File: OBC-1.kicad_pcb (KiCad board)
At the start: 6 copper layers, 42.8 x 42.8 mm, 110 parts, among them J1 ERM8-020-X, J2 ERF6-020-X, J3 Conn_01x02_Female, Q1 MGSF1N02L, Q2 MGSF1N02L, U1 TPS62850x-Q1, U11 TMS5701227CZWTQQ1, U2 TPS62850x-Q1, U3 LTC4353, U4 SN65HVD230M-EP, U5 SN65HVD230M-EP, U6 SN65HVD230M-EP

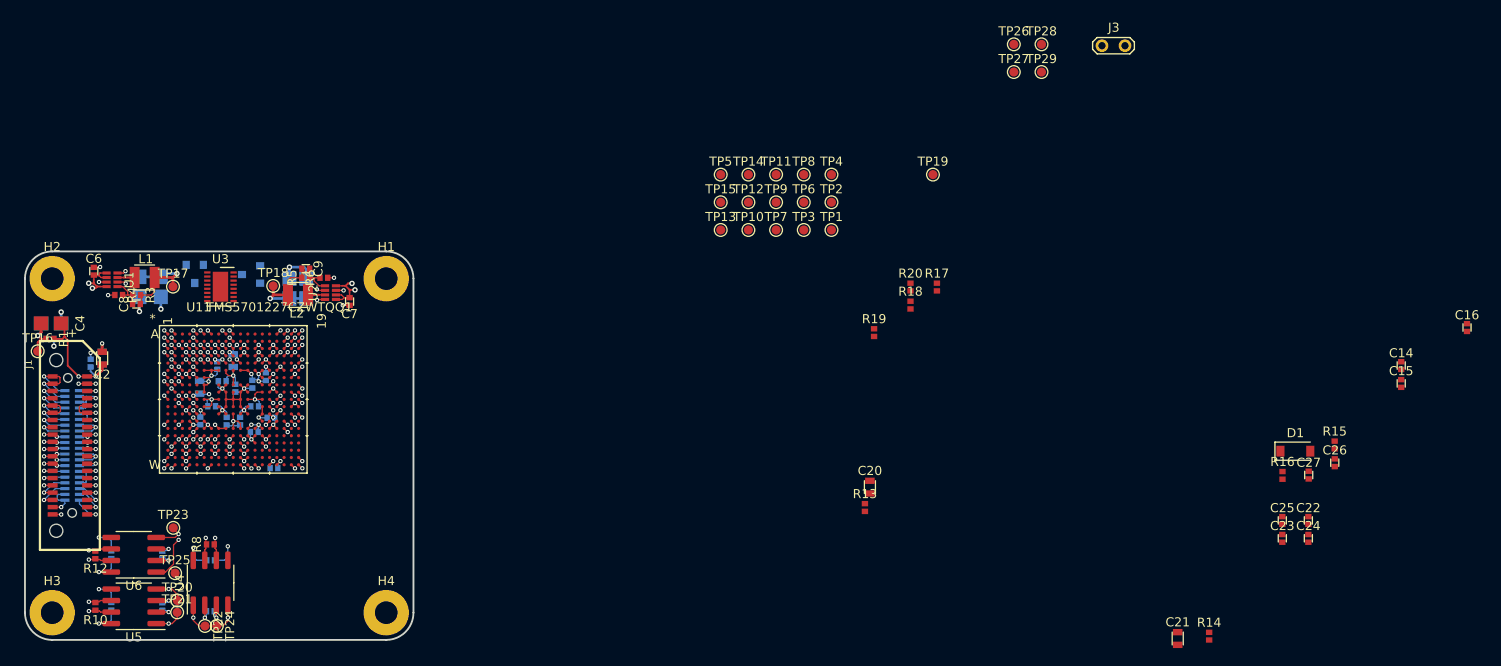
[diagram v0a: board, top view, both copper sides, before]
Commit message: progressed power supply layout, added 3D models to footprints
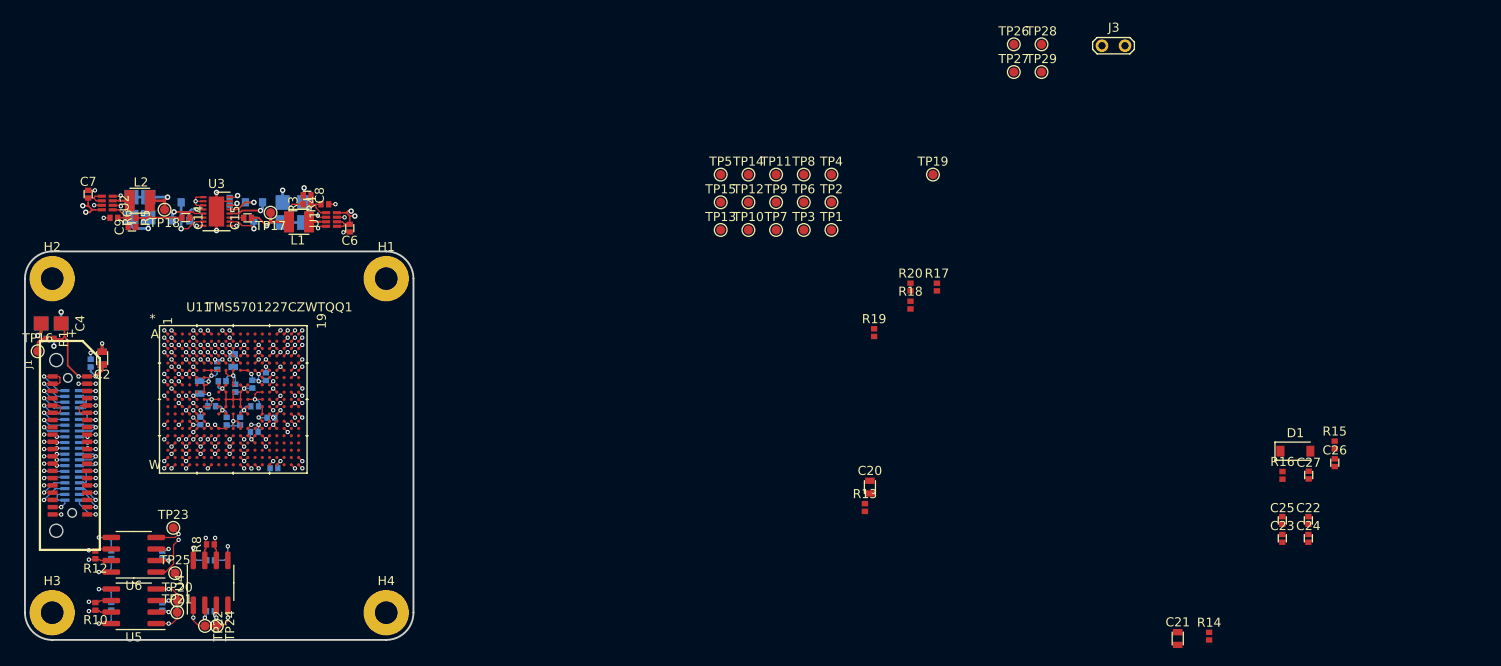
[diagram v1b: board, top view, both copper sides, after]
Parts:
- C16: moved to B.Cu
- moved C16 137.0 mm to (111.5, 66.0), turned to 180 degrees
- moved C14 134.9 mm to (106.6, 67.8), turned to 270 degrees
- moved C15 128.4 mm to (113.5, 67.8), turned to 90 degrees
- moved C7 31.1 mm to (95.9, 65.2), turned to 0 degrees
- moved C6 28.6 mm to (124.7, 68.9), turned to 180 degrees
- moved U2 28.2 mm to (97.4, 65.4), turned to 270 degrees
- moved U1 25.9 mm to (123.3, 68.7), turned to 90 degrees
- moved R4 24.8 mm to (121.9, 66.3), turned to 90 degrees
- moved R6 24.1 mm to (98.7, 67.8), turned to 270 degrees
- moved C8 22.3 mm to (120.0, 65.3), turned to 270 degrees
- moved R3 21.2 mm to (120.0, 66.3), turned to 90 degrees
- moved C11 21.2 mm to (100.6, 66.6), turned to 180 degrees
- moved L2 20.3 mm to (101.6, 65.9), turned to 0 degrees
- moved R5 20.3 mm to (100.7, 67.8), turned to 270 degrees
- moved C10 19.9 mm to (119.7, 67.2), turned to 0 degrees
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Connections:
- U11 pad C1: /TMS570_uC/OBC_1V25_P_PG -> /Power/OBC_1V25_P_PG
- U11 pad C2: /TMS570_uC/OBC_1V25_R_PG -> /Power/OBC_1V25_R_PG
- U3 pad 8: /Power/OBC_1V2_R_PG -> /Power/OBC_1V25_R_PG
- U3 pad 9: /Power/OBC_1V2_P_PG -> /Power/OBC_1V25_P_PG
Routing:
- net GND: track 178.0 -> 190.0 mm, vias 119 -> 123
- net OBC_1V2_R: track 11.4 -> 21.4 mm, vias 1 -> 2
- net OBC_1V25: track 19.5 -> 29.1 mm, vias 4 -> 6
- net OBC_1V25_P: track 12.0 -> 21.3 mm, vias 1 -> 2
- net /Power/GATE_1: track 0.00 -> 4.53 mm, vias 0 -> 1
- net /Power/GATE_2: track 0.00 -> 4.32 mm, vias 0 -> 1
- net OBC_3V3: track 65.6 -> 67.4 mm, vias 23 -> 24
- net Net-(C15-Pad2): track 0.00 -> 1.56 mm
- net Net-(C14-Pad2): track 0.00 -> 1.50 mm
- net /Power/OBC_1V25_P_PG: track 0.00 -> 1.31 mm, vias 0 -> 2
- net /Power/OBC_1V25_R_PG: track 0.00 -> 1.29 mm, vias 0 -> 2
- net /TMS570_uC/OBC_1V25_R_PG: track 0.57 -> 0.00 mm, vias 1 -> 0
- net /TMS570_uC/OBC_1V25_P_PG: track 0.56 -> 0.00 mm, vias 1 -> 0

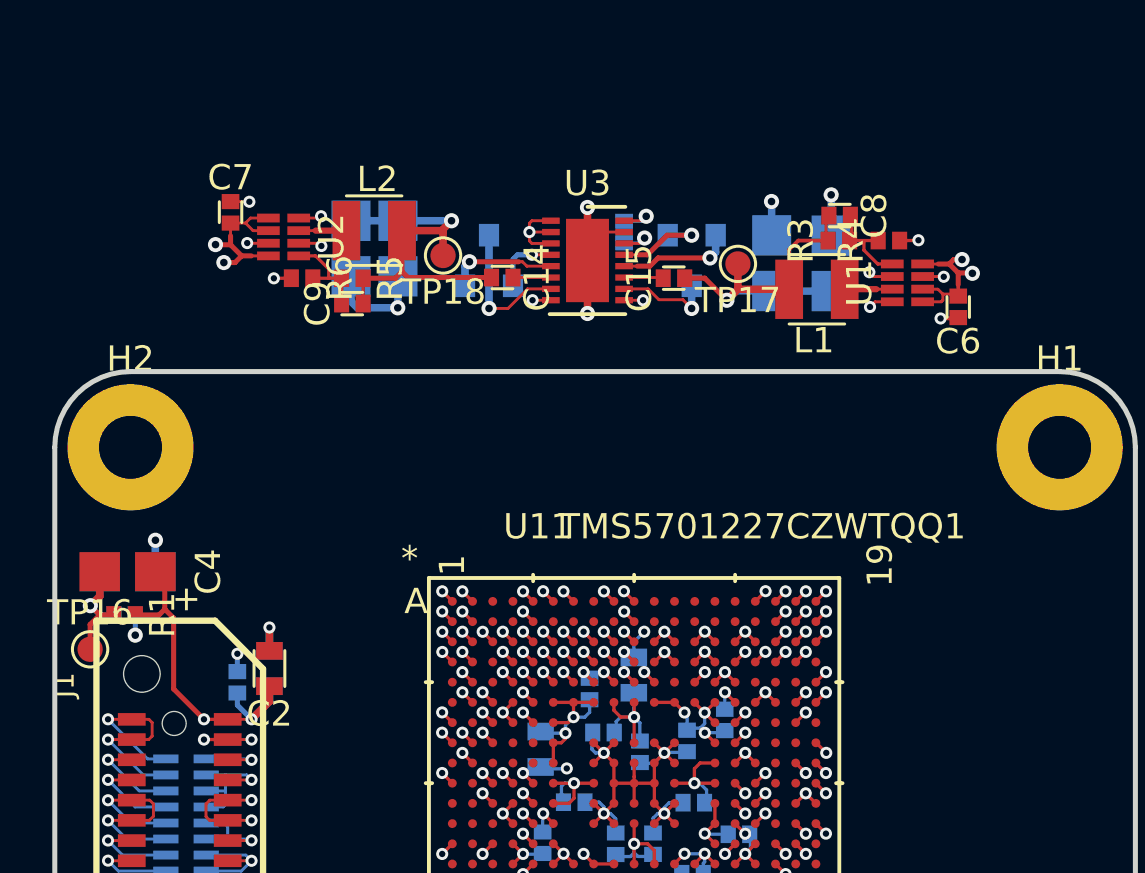
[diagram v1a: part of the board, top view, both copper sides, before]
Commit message: updated power planes
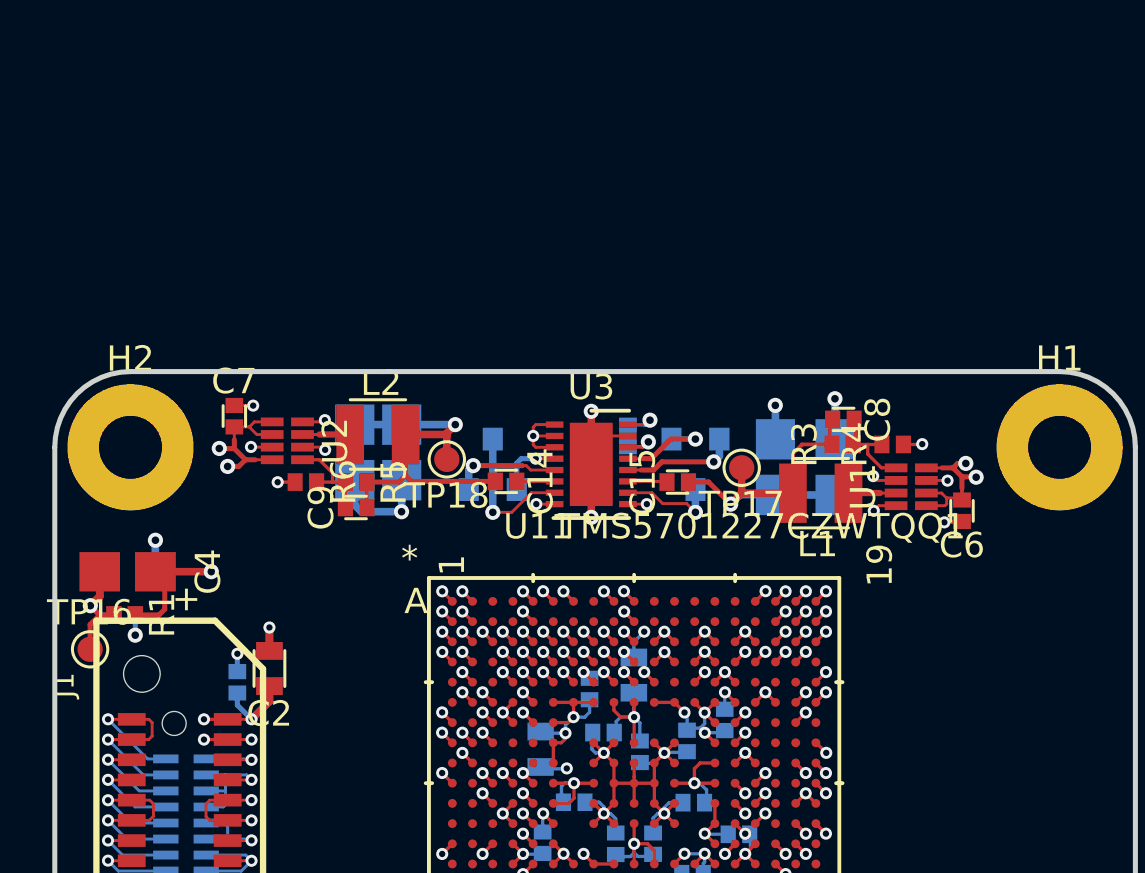
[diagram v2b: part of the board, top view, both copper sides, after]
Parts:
- moved C10 8.08 mm to (119.8, 75.3)
- moved C11 8.08 mm to (100.8, 74.7)
- moved C12 8.08 mm to (117.4, 75.3)
- moved C13 8.08 mm to (102.6, 74.7)
- moved C15 8.08 mm to (113.6, 75.9)
- moved C16 8.08 mm to (111.6, 74.1)
- moved C6 8.08 mm to (124.8, 77.0)
- moved C7 8.08 mm to (96.0, 73.3)
- moved C8 8.08 mm to (120.1, 73.4)
- moved C9 8.08 mm to (100.9, 76.9)
- moved L1 8.08 mm to (119.2, 76.3)
- moved Q1 8.08 mm to (106.2, 75.2)
- moved Q2 8.08 mm to (114.3, 75.2)
- moved R3 8.08 mm to (120.1, 74.4)
- moved R4 8.08 mm to (122.1, 74.4)
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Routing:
- net OBC_3V3: track 67.4 -> 64.6 mm, vias 24 -> 25
- removed copper zone on In3.Cu, net OBC_3V3

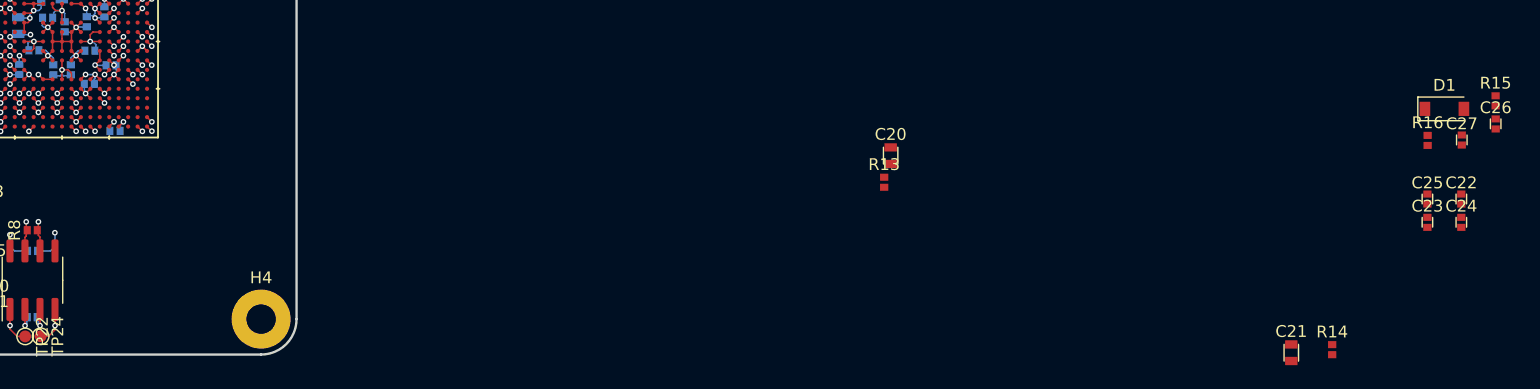
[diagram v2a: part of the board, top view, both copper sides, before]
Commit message: initial supervisor layout, needs XTAL adding
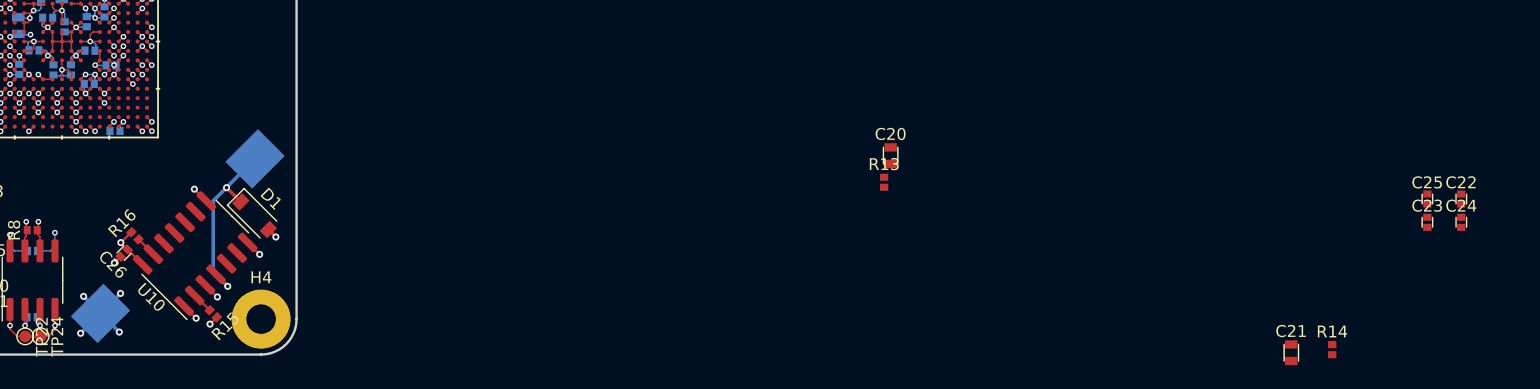
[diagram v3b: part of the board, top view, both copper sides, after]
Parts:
- added U10: FM33256B, Package_SO:SOIC-14_3.9x8.7mm_P1.27mm, F.Cu at (123.1, 105.8)
- C27: footprint TFT_C_passive_SMD:0402_CAP -> TFT_C_passive_SMD:MAL219691152E3_short; moved to B.Cu
- moved C26 116.6 mm to (117.1, 105.7), turned to 135 degrees
- moved R15 110.0 mm to (124.7, 110.8), turned to 225 degrees
- moved R16 109.7 mm to (118.0, 104.2), turned to 45 degrees
- moved C27 109.0 mm to (121.7, 104.3), turned to 225 degrees
- moved D1 101.1 mm to (128.2, 102.5), turned to 315 degrees
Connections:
- net OBC_1V2_R renamed OBC_1V25_R
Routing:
- net OBC_RTC_Vbackup: track 0.00 -> 15.9 mm, vias 0 -> 2
- net GND: track 190.0 -> 203.6 mm, vias 123 -> 131
- net OBC_3V3: track 64.6 -> 68.5 mm, vias 25 -> 26
- net Net-(R15-Pad2): track 0.00 -> 1.79 mm
- net /Supervisor_RTC_FRAM/SPVSR_ACS: track 0.57 -> 2.34 mm
- net /Supervisor_RTC_FRAM/SPVSR_nCS: track 0.57 -> 2.01 mm, vias 1 -> 2
- net /Supervisor_RTC_FRAM/SPVSR_CNT: track 0.57 -> 2.01 mm, vias 1 -> 2
- net /Supervisor_RTC_FRAM/SPVSR_CIPO: track 0.56 -> 1.38 mm, vias 1 -> 2

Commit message: completed supervisor layout
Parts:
- added X1: ASTMTXK-32.768KHZ, TFT_BGA:ASTMTXK_OSC, F.Cu at (127.6, 107.3)
- moved J3 109.2 mm to (118.7, 112.3)
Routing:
- net OBC_3V3: track 68.5 -> 80.3 mm, vias 26 -> 27
- net OBC_RTC_Vbackup: track 15.9 -> 22.3 mm
- net Net-(U10-Pad6): track 0.00 -> 1.61 mm
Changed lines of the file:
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@@
     (thickness 1.6)
     (drawings 8)
-    (tracks 1412)
+    (tracks 1424)
     (zones 0)
-    (modules 111)
+    (modules 112)
     (nets 223)
   )
@@
   )
   (setup
-    (last_trace_width 0.2)
+    (last_trace_width 0.3)
     (user_trace_width 0.1)
     (user_trace_width 0.115)
@@
     (add_net PAYLOAD_5V)
   )
+  (module TFT_BGA:ASTMTXK_OSC (layer F.Cu)
+    (at 127.6 107.35 45)
+    (fp_text reference X1 (at 0.2032 -3.8608 45) (layer F.SilkS)
+      (effects (font (size 1 1) (thickness 0.15)))
+    )
+    (fp_text value ASTMTXK-32.768KHZ (at 0.2286 -5.461 45) (layer F.Fab)
+      (effects (font (size 1 1) (thickness 0.15)))
+    )
+    (fp_line (start -0.752 -0.42) (end 0.752 -0.42) (layer F.SilkS) (width 0.06))
+    (fp_line (start 0.752 -0.42) (end 0.752 0.42) (layer F.SilkS) (width 0.06))
+    (fp_line (start 0.752 0.42) (end -0.752 0.42) (layer F.SilkS) (width 0.06))
+    (fp_line (start -0.752 0.42) (end -0.752 -0.42) (layer F.SilkS) (width 0.06))
+    (fp_circle (center -0.9 0.6) (end -0.82 0.6) (layer F.SilkS) (width 0.06))
+    (fp_line (start -0.752 -0.42) (end -0.752 0.42) (layer F.CrtYd) (width 0.06))
+    (fp_line (start -0.752 0.42) (end 0.752 0.42) (layer F.CrtYd) (width 0.06))
+    (fp_line (start 0.752 0.42) (end 0.752 -0.42) (layer F.CrtYd) (width 0.06))
+    (fp_line (start 0.752 -0.42) (end -0.752 -0.42) (layer F.CrtYd) (width 0.06))
+    (pad 4 smd circle (at -0.5 -0.205 45) (size 0.25 0.25) (layers F.Cu F.Paste F.Mask)
+      (net 1 OBC_3V3) (solder_mask_margin 0.05))
+    (pad 3 smd circle (at 0.5 -0.205 45) (size 0.25 0.25) (layers F.Cu F.Paste F.Mask)
+      (net 221 "Net-(U10-Pad6)") (solder_mask_margin 0.05))
+    (pad 2 smd circle (at 0.5 0.205 45) (size 0.25 0.25) (layers F.Cu F.Paste F.Mask)
+      (net 2 GND) (solder_mask_margin 0.05))
+    (pad 1 smd circle (at -0.5 0.205 45) (size 0.25 0.25) (layers F.Cu F.Paste F.Mask)
+      (net 2 GND) (solder_mask_margin 0.05))
+  )
   (module Package_SO:SOIC-14_3.9x8.7mm_P1.27mm (layer F.Cu)
     (at 123.124911 105.753859 135)
@@
   )
   (module TFT_TestPoints:TP_2Pads_Pitch2.54mm_Drill0.8mm (layer F.Cu)
-    (at 207.5483 48.8382)
+    (at 118.68 112.26)
     (descr "Test point with 2 pins, pitch 2.54mm, drill diameter 0.8mm")
     (tags "CONN DEV")
@@
   (segment (start 117.70052 103.94948) (end 116.825 104.825) (width 0.2) (layer F.Cu) (net 1))
   (segment (start 117.72448 103.94948) (end 117.70052 103.94948) (width 0.2) (layer F.Cu) (net 1))
+  (segment (start 127.101403 107.558597) (end 126.69 107.97) (width 0.1) (layer F.Cu) (net 1))
+  (via (at 126.69 107.97) (size 0.48) (drill 0.25) (layers F.Cu B.Cu) (net 1))
+  (segment (start 127.10149 107.558597) (end 127.101403 107.558597) (width 0.1) (layer F.Cu) (net 1))
+  (segment (start 126.544999 107.824999) (end 126.69 107.97) (width 0.5) (layer In2.Cu) (net 1))
+  (segment (start 121.235001 107.824999) (end 126.544999 107.824999) (width 0.5) (layer In2.Cu) (net 1))
+  (segment (start 119.83 107.83) (end 121.23 107.83) (width 0.5) (layer In2.Cu) (net 1))
+  (segment (start 121.23 107.83) (end 121.235001 107.824999) (width 0.5) (layer In2.Cu) (net 1))
+  (segment (start 116.825 104.825) (end 119.83 107.83) (width 0.5) (layer In2.Cu) (net 1))
   (segment (start 107.04636 83.80272) (end 107.045393 83.80272) (width 0.13) (layer F.Cu) (net 2))
   (via (at 110.64748 86.60384) (size 0.48) (drill 0.25) (layers F.Cu B.Cu) (net 2))
@@
   (segment (start 124.65 101.3) (end 124.65 107.300014) (width 0.3) (layer B.Cu) (net 8))
   (segment (start 125.775 100.175) (end 124.65 101.3) (width 0.3) (layer B.Cu) (net 8))
+  (segment (start 121.22 110.730014) (end 124.65 107.300014) (width 0.3) (layer B.Cu) (net 8))
+  (segment (start 121.22 112.26) (end 121.22 110.730014) (width 0.3) (layer B.Cu) (net 8))
   (via (at 96.69384 88.47328) (size 0.48) (drill 0.25) (layers F.Cu B.Cu) (net 9))
   (segment (start 96.69212 88.475) (end 96.69384 88.47328) (width 0.115) (layer F.Cu) (net 9))
@@
   (segment (start 107.975256 76.75) (end 107.972756 76.7475) (width 0.115) (layer F.Cu) (net 218))
   (segment (start 108.7 76.75) (end 107.975256 76.75) (width 0.115) (layer F.Cu) (net 218))
+  (segment (start 126.671052 105.713945) (end 126.671052 105.707897) (width 0.1) (layer F.Cu) (net 221))
+  (segment (start 127.808597 106.85149) (end 126.671052 105.713945) (width 0.1) (layer F.Cu) (net 221))
   (zone (net 2) (net_name GND) (layer In1_GND.Cu) (hatch edge 0.508)
     (connect_pads (clearance 0.3))
